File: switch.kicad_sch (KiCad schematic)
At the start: 0 parts

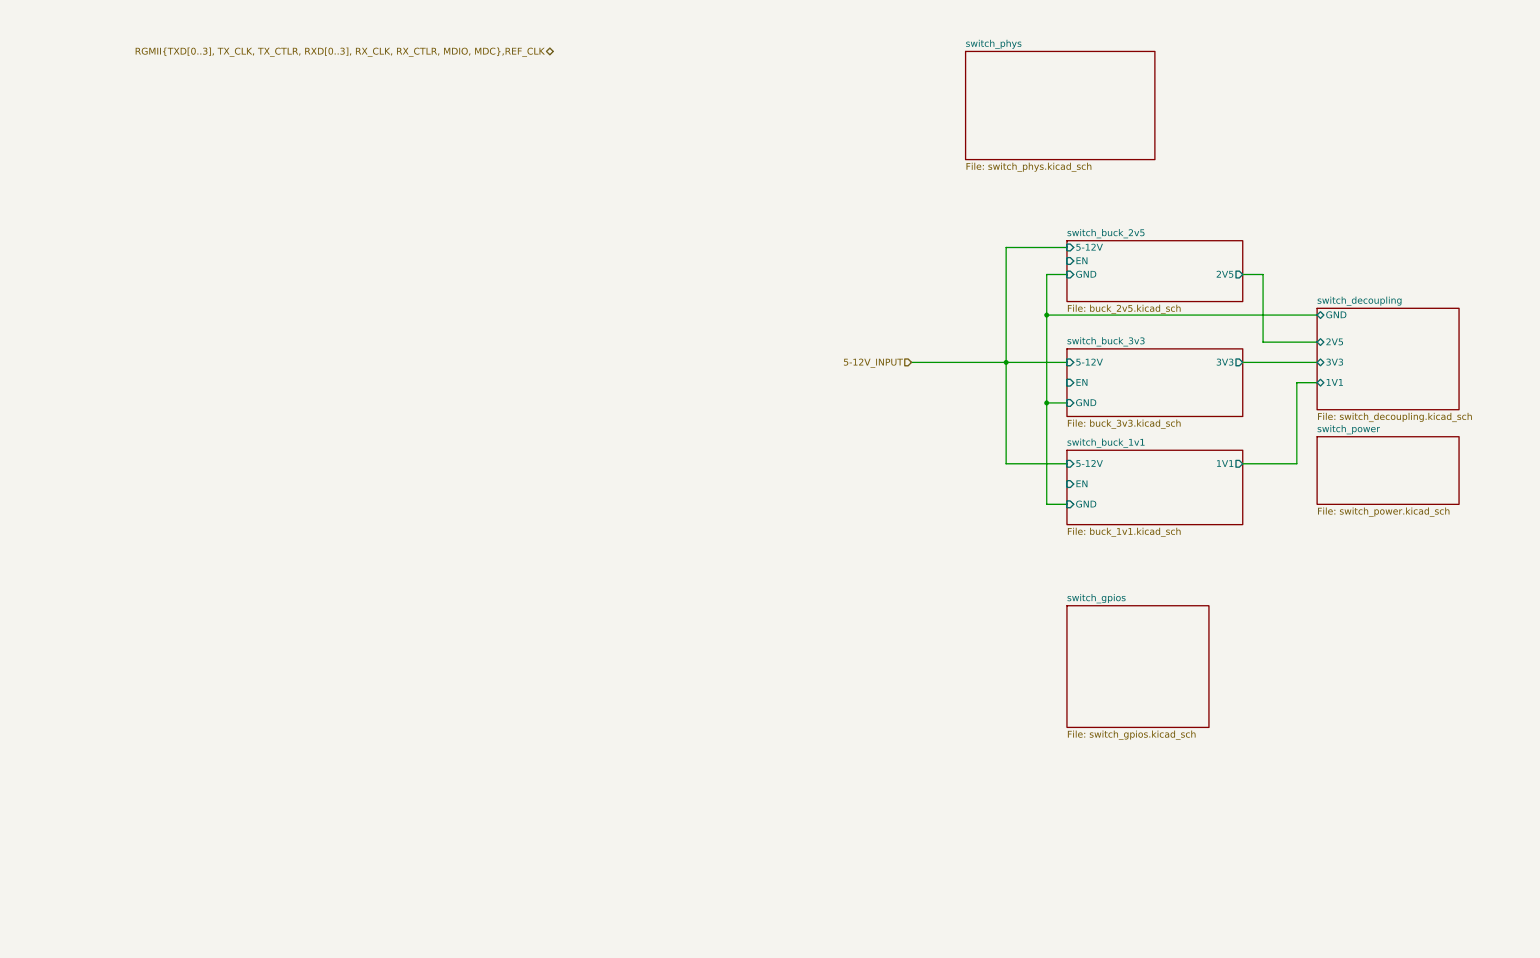
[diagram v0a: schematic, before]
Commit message: switch: Connecting bucks/gpios/phys together
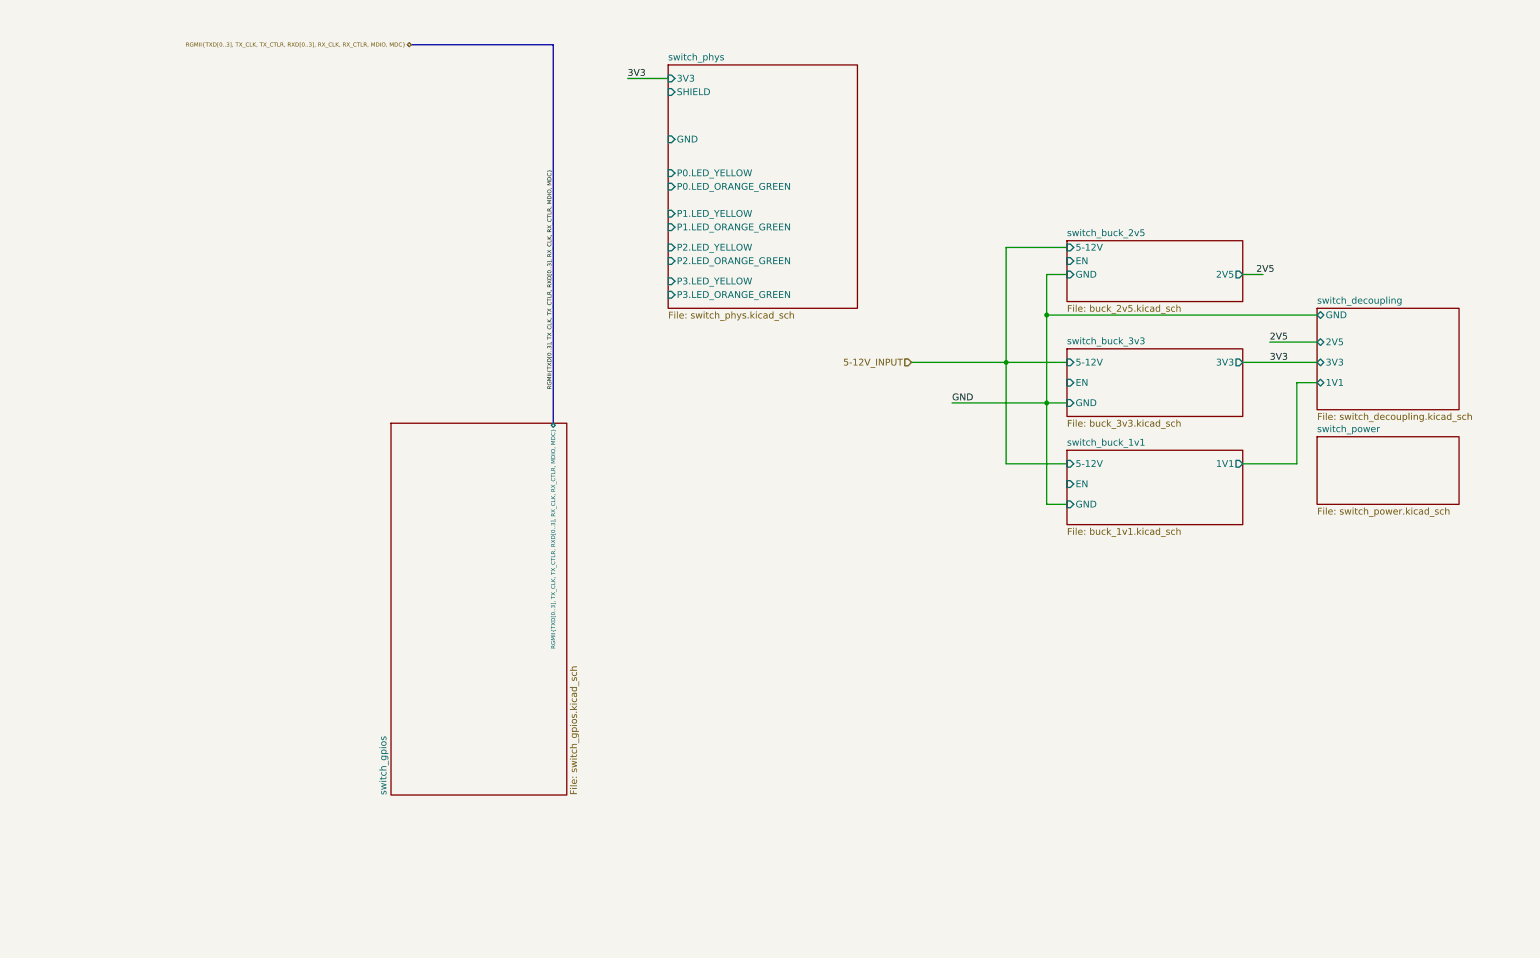
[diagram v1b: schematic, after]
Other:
- sheet switch_gpios ports: added RGMII{TXD[0..3], TX_CLK, TX_CTLR, RXD[0..3], RX_CLK, RX_CTLR, MDIO, MDC}; removed none
- sheet switch_phys ports: added 3V3, GND, P0.LED_ORANGE_GREEN, P0.LED_YELLOW, P1.LED_ORANGE_GREEN, P1.LED_YELLOW, P2.LED_ORANGE_GREEN, P2.LED_YELLOW, P3.LED_ORANGE_GREEN, P3.LED_YELLOW, SHIELD; removed none
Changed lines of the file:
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@@
-	(wire
-		(pts
-			(xy 232.41 77.47) (xy 242.57 77.47)
-		)
-		(stroke
-			(width 0)
-			(type default)
-		)
-	)
-	(wire
-		(pts
-			(xy 232.41 64.77) (xy 232.41 77.47)
-		)
-		(stroke
-			(width 0)
-			(type default)
-		)
-	)
 	(wire
 		(pts
@@
 		)
 	)
+	(bus
+		(pts
+			(xy 99.06 21.59) (xy 99.06 92.71)
+		)
+		(stroke
+			(width 0)
+			(type default)
+		)
+	)
 	(wire
 		(pts
@@
 		)
 	)
+	(bus
+		(pts
+			(xy 99.06 21.59) (xy 72.39 21.59)
+		)
+		(stroke
+			(width 0)
+			(type default)
+		)
+	)
 	(wire
 		(pts
@@
 	(wire
 		(pts
+			(xy 113.03 27.94) (xy 120.65 27.94)
+		)
+		(stroke
+			(width 0)
+			(type default)
+		)
+	)
+	(wire
+		(pts
 			(xy 191.77 64.77) (xy 195.58 64.77)
 		)
@@
 	(wire
 		(pts
+			(xy 173.99 88.9) (xy 191.77 88.9)
+		)
+		(stroke
+			(width 0)
+			(type default)
+		)
+	)
+	(wire
+		(pts
 			(xy 191.77 107.95) (xy 191.77 88.9)
 		)
@@
 	(wire
 		(pts
+			(xy 233.68 77.47) (xy 242.57 77.47)
+		)
+		(stroke
+			(width 0)
+			(type default)
+		)
+	)
+	(wire
+		(pts
 			(xy 166.37 81.28) (xy 184.15 81.28)
 		)
@@
 			(width 0)
 			(type default)
+		)
+	)
+	(label "RGMII{TXD[0..3], TX_CLK, TX_CTLR, RXD[0..3], RX_CLK, RX_CTLR, MDIO, MDC}"
+		(at 99.06 86.36 90)
+		(effects
+			(font
+				(size 0.762 0.762)
+			)
+			(justify left bottom)
+		)
+	)
+	(label "3V3"
+		(at 113.03 27.94 0)
+		(effects
+			(font
+				(size 1.27 1.27)
+			)
+			(justify left bottom)
+		)
+	)
+	(label "3V3"
+		(at 233.68 81.28 0)
+		(effects
+			(font
+				(size 1.27 1.27)
+			)
+			(justify left bottom)
+		)
+	)
+	(label "2V5"
+		(at 233.68 77.47 0)
+		(effects
+			(font
+				(size 1.27 1.27)
+			)
+			(justify left bottom)
+		)
+	)
+	(label "2V5"
+		(at 231.14 64.77 0)
+		(effects
+			(font
+				(size 1.27 1.27)
+			)
+			(justify left bottom)
+		)
+	)
+	(label "GND"
+		(at 173.99 88.9 0)
+		(effects
+			(font
+				(size 1.27 1.27)
+			)
+			(justify left bottom)
 		)
 	)
@@
 		)
 	)
-	(hierarchical_label "RGMII{TXD[0..3], TX_CLK, TX_CTLR, RXD[0..3], RX_CLK, RX_CTLR, MDIO, MDC},REF_CLK"
+	(hierarchical_label "RGMII{TXD[0..3], TX_CLK, TX_CTLR, RXD[0..3], RX_CLK, RX_CTLR, MDIO, MDC}"
 		(shape bidirectional)
-		(at 99.06 22.86 180)
+		(at 72.39 21.59 180)
 		(effects
 			(font
-				(size 1.27 1.27)
+				(size 0.762 0.762)
 			)
 			(justify right)
@@
 	)
 	(sheet
-		(at 195.58 127)
-		(size 26.67 22.86)
+		(at 68.58 92.71)
+		(size 33.02 69.85)
 		(exclude_from_sim no)
 		(in_bom yes)
@@
 		)
 		(property "Sheetname" "switch_gpios"
-			(at 195.58 126.2884 0)
+			(at 67.8684 162.56 90)
 			(effects
 				(font
@@
 		)
 		(property "Sheetfile" "switch_gpios.kicad_sch"
-			(at 195.58 150.4446 0)
+			(at 102.1846 162.56 90)
 			(effects
 				(font
@@
 				)
 				(justify left top)
+			)
+		)
+		(pin "RGMII{TXD[0..3], TX_CLK, TX_CTLR, RXD[0..3], RX_CLK, RX_CTLR, MDIO, MDC}"
+			bidirectional
+			(at 99.06 92.71 90
+			)
+			(effects
+				(font
+					(size 0.762 0.762)
+				)
+				(justify right)
 			)
 		)
@@
 	)
 	(sheet
-		(at 176.53 22.86)
-		(size 35.56 20.32)
+		(at 120.65 25.4)
+		(size 35.56 45.72)
 		(exclude_from_sim no)
 		(in_bom yes)
@@
 		)
 		(property "Sheetname" "switch_phys"
-			(at 176.53 22.1484 0)
+			(at 120.65 24.6884 0)
 			(effects
 				(font
@@
 		)
 		(property "Sheetfile" "switch_phys.kicad_sch"
-			(at 176.53 43.7646 0)
+			(at 120.65 71.7046 0)
 			(effects
 				(font
@@
 			)
 		)
+		(pin "P2.LED_ORANGE_GREEN" input
+			(at 120.65 62.23 180)
+			(effects
+				(font
+					(size 1.27 1.27)
+				)
+				(justify left)
+			)
+		)
+		(pin "3V3" input
+			(at 120.65 27.94 180)
+			(effects
+				(font
+					(size 1.27 1.27)
+				)
+				(justify left)
+			)
+		)
+		(pin "P1.LED_YELLOW" input
+			(at 120.65 53.34 180)
+			(effects
+				(font
+					(size 1.27 1.27)
+				)
+				(justify left)
+			)
+		)
+		(pin "P0.LED_ORANGE_GREEN" input
+			(at 120.65 48.26 180)
+			(effects
+				(font
+					(size 1.27 1.27)
+				)
+				(justify left)
+			)
+		)
+		(pin "P1.LED_ORANGE_GREEN" input
+			(at 120.65 55.88 180)
+			(effects
+				(font
+					(size 1.27 1.27)
+				)
+				(justify left)
+			)
+		)
+		(pin "P0.LED_YELLOW" input
+			(at 120.65 45.72 180)
+			(effects
+				(font
+					(size 1.27 1.27)
+				)
+				(justify left)
+			)
+		)
+		(pin "P2.LED_YELLOW" input
+			(at 120.65 59.69 180)
+			(effects
+				(font
+					(size 1.27 1.27)
+				)
+				(justify left)
+			)
+		)
+		(pin "P3.LED_YELLOW" input
+			(at 120.65 66.04 180)
+			(effects
+				(font
+					(size 1.27 1.27)
+				)
+				(justify left)
+			)
+		)
+		(pin "SHIELD" input
+			(at 120.65 30.48 180)
+			(effects
+				(font
+					(size 1.27 1.27)
+				)
+				(justify left)
+			)
+		)
+		(pin "GND" input
+			(at 120.65 39.37 180)
+			(effects
+				(font
+					(size 1.27 1.27)
+				)
+				(justify left)
+			)
+		)
+		(pin "P3.LED_ORANGE_GREEN" input
+			(at 120.65 68.58 180)
+			(effects
+				(font
+					(size 1.27 1.27)
+				)
+				(justify left)
+			)
+		)

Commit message: schematics: fixing the voltage rail and updating the files
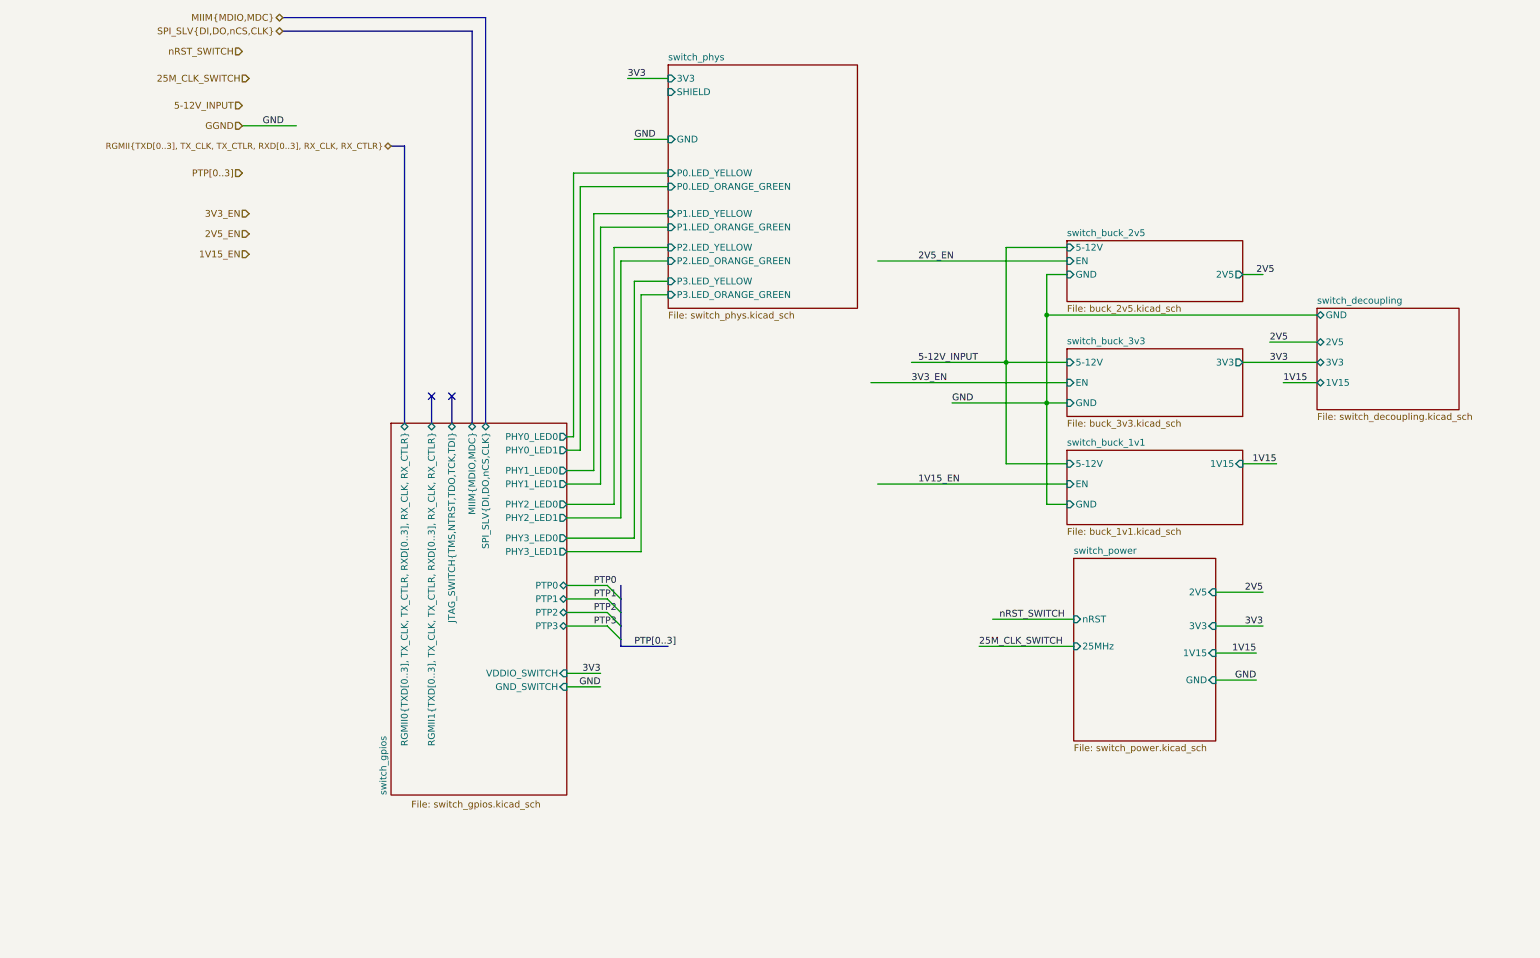
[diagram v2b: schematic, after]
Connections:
- no-connect marks 0 -> 2
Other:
- sheet switch_buck_1v1 ports: added 1V15; removed 1V1
- sheet switch_decoupling ports: added 1V15; removed 1V1
- sheet switch_gpios ports: added GND_SWITCH, JTAG_SWITCH{TMS,NTRST,TDO,TCK,TDI}, MIIM{MDIO,MDC}, PHY0_LED0, PHY0_LED1, PHY1_LED0, PHY1_LED1, PHY2_LED0, PHY2_LED1, PHY3_LED0, PHY3_LED1, PTP0, PTP1, PTP2, PTP3, RGMII0{TXD[0..3], TX_CLK, TX_CTLR, RXD[0..3], RX_CLK, RX_CTLR}, RGMII1{TXD[0..3], TX_CLK, TX_CTLR, RXD[0..3], RX_CLK, RX_CTLR}, SPI_SLV{DI,DO,nCS,CLK}, VDDIO_SWITCH; removed RGMII{TXD[0..3], TX_CLK, TX_CTLR, RXD[0..3], RX_CLK, RX_CTLR, MDIO, MDC}
- sheet switch_power ports: added 1V15, 25MHz, 2V5, 3V3, GND, nRST; removed none

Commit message: switch: finished 1st version
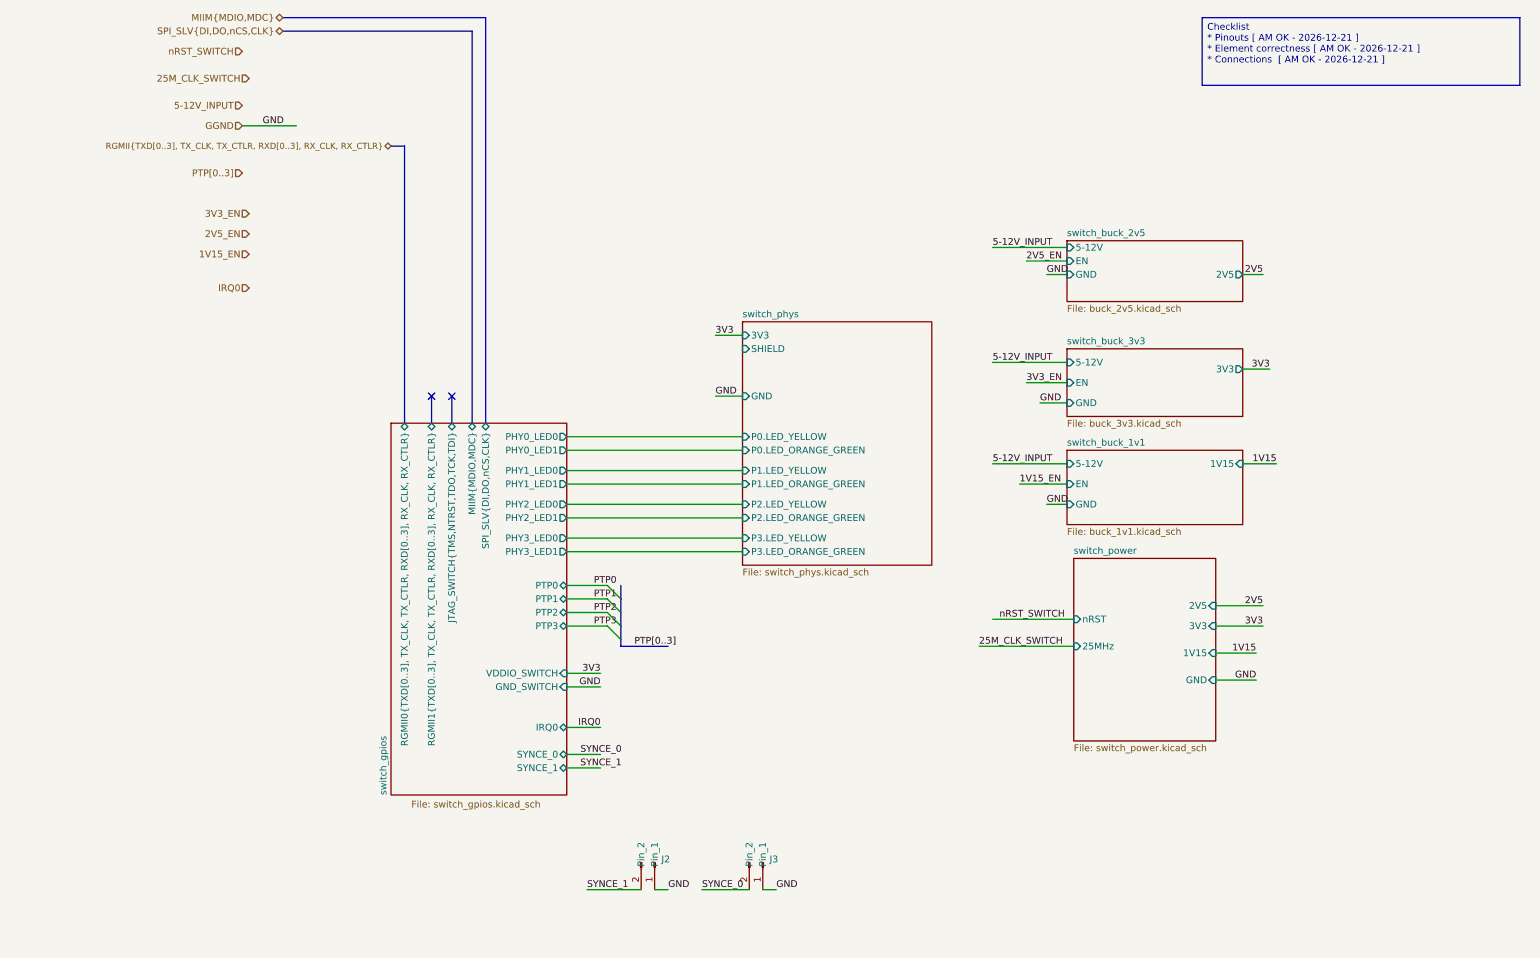
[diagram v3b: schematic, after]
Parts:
- added J2, J3: ~, KL:PinHeader_1x2_2.54mm, symbol KL_Connector_Headers:1x2_Pin_Header
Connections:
- net GGND: now also J2.1 (Pin_1), J3.1 (Pin_1)
- new net SYNCE_0: J3.2 (Pin_2)
- new net SYNCE_1: J2.2 (Pin_2)
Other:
- removed sheet switch_decoupling
- sheet switch_gpios ports: added IRQ0, SYNCE_0, SYNCE_1; removed none
- company: (none) -> Kebag-Logic <contact@kebag-logic.com>
- title: (none) -> Switch Top Level

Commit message: minor footprint fixing
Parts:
- added U1: ~, KL:TQFP-128_14x14mm_P0.4mm_with_EPAD, symbol KL_IC_LAN9645xF:lan9645xF_128_TQFP
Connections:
- no-connect marks 2 -> 12
